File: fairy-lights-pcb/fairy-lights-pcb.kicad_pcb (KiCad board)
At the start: 2 copper layers, 60 x 60 mm, 18 parts, among them J1 Power_Jack, J2 Conn_LED_Strand, J3 Conn_LED_Strand, J4 Conn_LED_Strand, J5 Conn_02x04_Top_Bottom, SW1 SW_PWR, SW2 SW_User, U1 WeMos_D1_mini, U2 TXS0108EPW

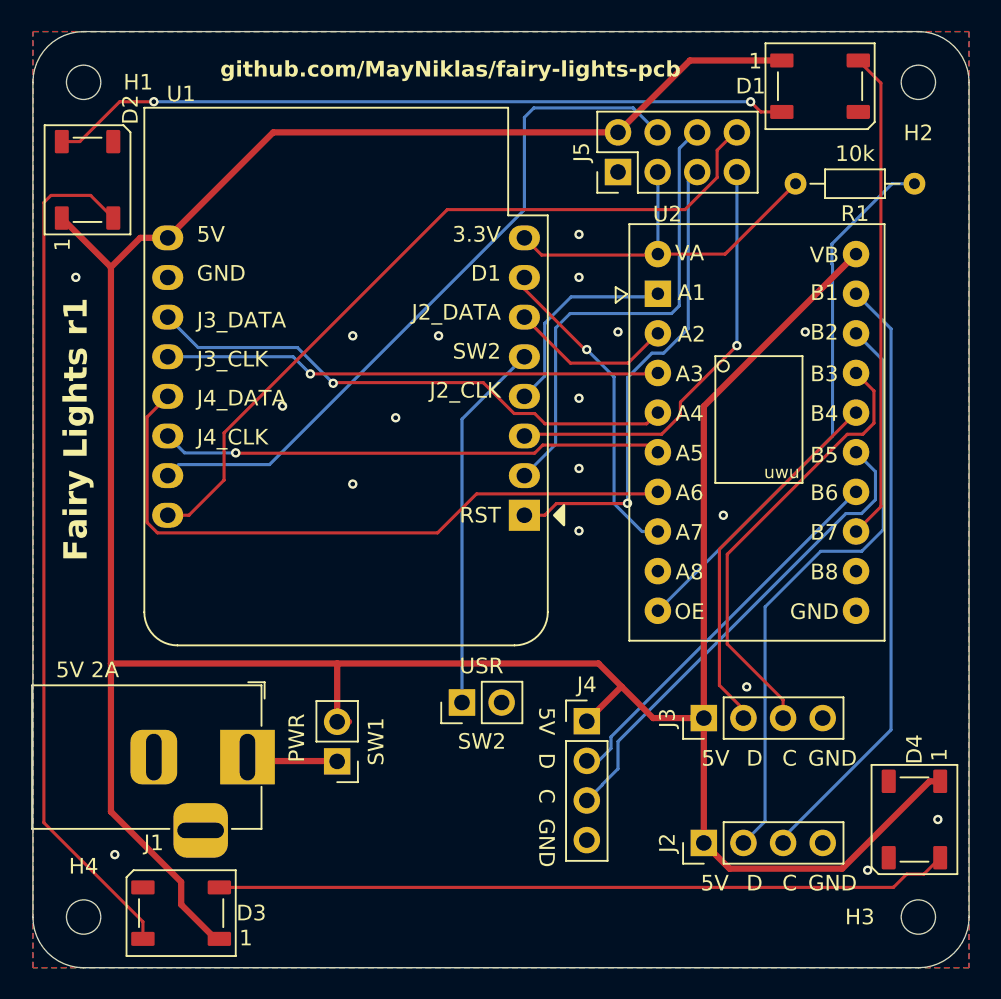
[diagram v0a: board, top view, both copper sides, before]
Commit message: Yeet level shifter; update interfaces
- The level shifter we planned to use seems not to work on a breadboard.
- Driving the LED controllers with 3.3V signals directly instead seems
  to work (although it is out-of-spec or barely at the boundary of what
  is in-spec).
- LED strands are now attached via screw terminals. (Of course, one can
  choose not to populate them and solder wires directly to the pads
  instead.)
- The size of one of the terminals is reduced to three signals, to
  accomodate WS2812 LED strands.
- The thus-free GPIO pin is repurposed to be another switch.
- Changed user switches to tactile vertical push buttons.
- Updated parts list in README.
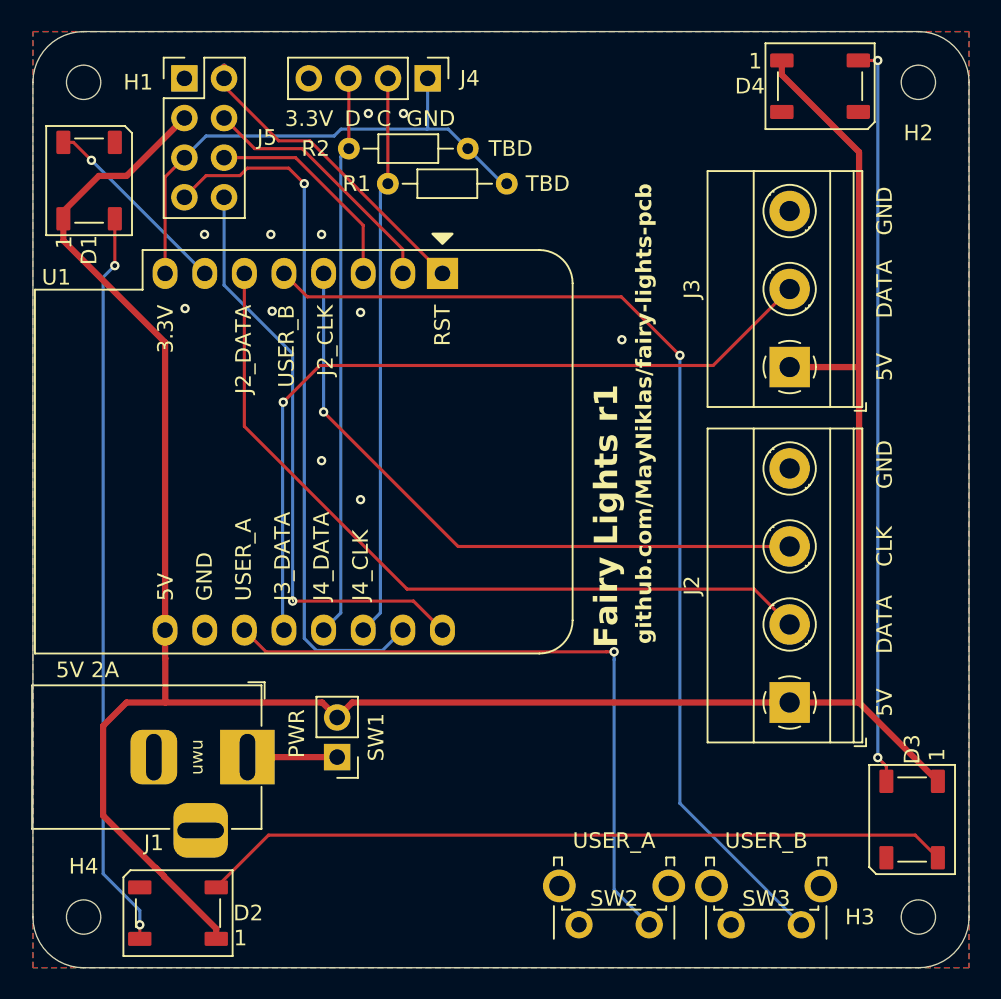
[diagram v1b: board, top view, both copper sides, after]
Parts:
- removed U2: TXS0108EPW, CustomLibrary:Texas_TXS0108E_Level_Shifter_Module
- added R2: TBD, Resistor_THT:R_Axial_DIN0204_L3.6mm_D1.6mm_P7.62mm_Horizontal, F.Cu at (87.9, 67.5)
- added SW3: USER_B, Button_Switch_THT:SW_Tactile_SPST_Angled_PTS645Vx31-2LFS, F.Cu at (109.2, 117.2)
- J2: value Conn_LED_Strand -> Conn_LED_Strand_SPI; footprint Connector_PinHeader_2.54mm:PinHeader_1x04_P2.54mm_Vertical -> TerminalBlock_Phoenix:TerminalBlock_Phoenix_MKDS-1,5-4_1x04_P5.00mm_Horizontal
- J3: value Conn_LED_Strand -> Conn_LED_Strand_WS2812; footprint Connector_PinHeader_2.54mm:PinHeader_1x04_P2.54mm_Vertical -> TerminalBlock_Phoenix:TerminalBlock_Phoenix_MKDS-1,5-3_1x03_P5.00mm_Horizontal
- J4: value Conn_LED_Strand -> Conn_I2C
- R1: value 10k -> TBD
- SW2: value SW_User -> USER_A; footprint Connector_PinHeader_2.54mm:PinHeader_1x02_P2.54mm_Vertical -> Button_Switch_THT:SW_Tactile_SPST_Angled_PTS645Vx31-2LFS
- moved D4 47.4 mm to (110.5, 63.5), turned to 0 degrees
- moved D2 47.4 mm to (69.3, 116.5), turned to 180 degrees
- moved D1 47.2 mm to (63.6, 69.5), turned to 90 degrees
- moved D3 47.2 mm to (116.3, 110.5), turned to -90 degrees
- moved J4 42.4 mm to (85.3, 63.0), turned to -90 degrees
- moved R1 33.8 mm to (82.8, 69.8), turned to 0 degrees
- moved J5 28.4 mm to (69.7, 63.0), turned to 0 degrees
- moved J3 23.2 mm to (108.5, 81.5)
- moved SW2 18.6 mm to (99.5, 117.2), turned to 180 degrees
- moved U1 16.4 mm to (86.2, 75.5), turned to -90 degrees
- moved J2 10.5 mm to (108.5, 103.0)
- moved SW1 0.28 mm to (79.5, 106.5)
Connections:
- J3 pad 3: Net-(J3-CLK) -> GND
- J4 pad 1: +5V -> +3.3V
- J4 pad 2: Net-(J4-DATA) -> Net-(J4-CLK)
- J4 pad 3: Net-(J4-CLK) -> Net-(J4-DATA)
- J5 pad 2: +5V -> UC_RST
- J5 pad 3: +3.3V -> +5V
- J5 pad 4: UC_RX -> UC_A0
- J5 pad 5: UC_RST -> +3.3V
- J5 pad 6: UC_A0 -> UC_D0
- J5 pad 7: UC_D0 -> UC_RX
- R1 pad 1: Net-(U2-OE) -> Net-(J4-CLK)
- SW2 pad 1: Net-(U1-MISO/D6) -> Net-(U1-D4)
- U1 pad 12: Net-(U1-D3) -> Net-(J3-DATA)
- U1 pad 13: Net-(U1-SDA/D2) -> Net-(J4-DATA)
- U1 pad 14: Net-(U1-SCL/D1) -> Net-(J4-CLK)
- U1 pad 4: Net-(U1-SCK/D5) -> Net-(J2-CLK)
- U1 pad 6: Net-(U1-MOSI/D7) -> Net-(J2-DATA)
- U1 pad 7: Net-(U1-CS/D8) -> Net-(D1-DIN)
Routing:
- net Net-(U1-MISO/D6): track 23.8 -> 67.3 mm, vias 0 -> 1
- net Net-(U1-SDA/D2): track 42.7 -> 0.00 mm
- net +5V: track 205.3 -> 165.9 mm
- net Net-(U2-OE): track 35.1 -> 0.00 mm
- net Net-(U1-SCL/D1): track 32.3 -> 0.00 mm, vias 1 -> 0
- net Net-(U1-D3): track 31.9 -> 0.00 mm, vias 1 -> 0
- net Net-(J3-CLK): track 28.6 -> 0.00 mm
- net Net-(J3-DATA): track 23.8 -> 50.1 mm, vias 0 -> 1
- net Net-(U1-CS/D8): track 20.5 -> 0.00 mm, vias 1 -> 0
- net Net-(D1-DIN): track 31.5 -> 12.5 mm, vias 0 -> 1
- net UC_A0: track 30.5 -> 16.5 mm
- net UC_D0: track 27.6 -> 13.8 mm, vias 1 -> 0
- net Net-(U1-SCK/D5): track 13.3 -> 0.00 mm
- net Net-(J2-DATA): track 38.6 -> 50.0 mm
- net UC_TX: track 49.4 -> 38.1 mm, vias 0 -> 1
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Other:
- board text added: "CLK"
- board text added: "DATA"
- board text added: "USER_A"
- board text added: "USER_B"
- board text removed: "D1"
- board text removed: "J3_CLK"
- board text removed: "SW2"
- board text removed: "USR"

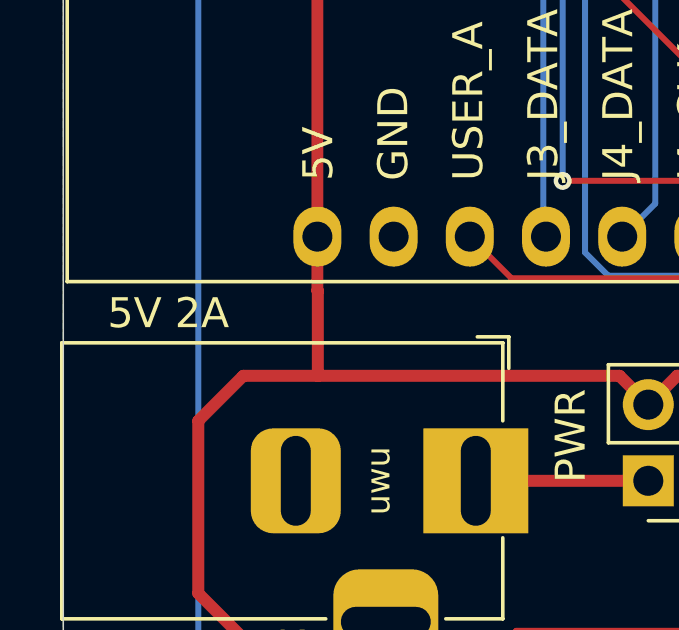
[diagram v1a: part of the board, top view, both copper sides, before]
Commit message: Ground the mounting pins of the buttons
Also tweaks the location of the "5V 2A" label.
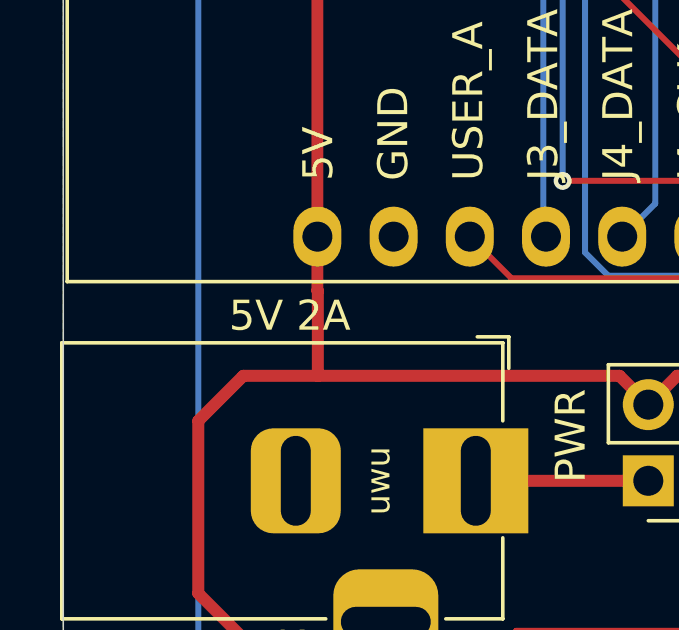
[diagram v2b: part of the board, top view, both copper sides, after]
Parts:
- SW2, SW3: footprint Button_Switch_THT:SW_Tactile_SPST_Angled_PTS645Vx31-2LFS -> CustomLibrary:SW_Tactile_SPST_Angled_PTS645Vx31-2LFS_2MP
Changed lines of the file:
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@@
 		)
 	)
-	(footprint "Button_Switch_THT:SW_Tactile_SPST_Angled_PTS645Vx31-2LFS"
+	(footprint "CustomLibrary:SW_Tactile_SPST_Angled_PTS645Vx31-2LFS_2MP"
 		(layer "F.Cu")
 		(at 99.5 117.2441 180)
@@
 		(tags "tactile switch SPST angled PTS645VL31-2 LFS C&K Button")
 		(property "Reference" "SW2"
-			(at 2.25 1.68 0)
+			(at 2.25 1.68 180)
 			(layer "F.SilkS")
 			(effects
@@
 		)
 		(property "Value" "USER_A"
-			(at 2.25 5.38988 0)
+			(at 2.25 5.38988 180)
 			(layer "F.SilkS")
 			(effects
@@
 			)
 		)
-		(property "Footprint" "Button_Switch_THT:SW_Tactile_SPST_Angled_PTS645Vx31-2LFS"
+		(property "Footprint" "CustomLibrary:SW_Tactile_SPST_Angled_PTS645Vx31-2LFS_2MP"
 			(at 0 0 180)
 			(unlocked yes)
@@
 			)
 		)
-		(property "Description" "Push button switch, generic, two pins"
+		(property "Description" "Generic push-button switch, two contact pins and shield pin(s)"
 			(at 0 0 180)
 			(unlocked yes)
@@
 		)
 		(fp_text user "${REFERENCE}"
-			(at 2.25 1.68 0)
+			(at 2.25 1.68 180)
 			(layer "F.Fab")
 			(effects
@@
 			)
 		)
-		(pad "" thru_hole circle
-			(at -1.25 2.49 180)
-			(size 2.1 2.1)
-			(drill 1.3)
-			(layers "*.Cu" "*.Mask")
-			(remove_unused_layers no)
-		)
-		(pad "" thru_hole circle
-			(at 5.76 2.49 180)
-			(size 2.1 2.1)
-			(drill 1.3)
-			(layers "*.Cu" "*.Mask")
-			(remove_unused_layers no)
-		)
 		(pad "1" thru_hole circle
 			(at 0 0 180)
@@
 			(pintype "passive")
 		)
+		(pad "3" thru_hole circle
+			(at -1.25 2.49 180)
+			(size 2.1 2.1)
+			(drill 1.3)
+			(layers "*.Cu" "*.Mask")
+			(remove_unused_layers no)
+			(net 2 "GND")
+			(pinfunction "SH1")
+			(pintype "passive")
+		)
+		(pad "4" thru_hole circle
+			(at 5.76 2.49 180)
+			(size 2.1 2.1)
+			(drill 1.3)
+			(layers "*.Cu" "*.Mask")
+			(remove_unused_layers no)
+			(net 2 "GND")
+			(pinfunction "SH2")
+			(pintype "passive")
+		)
 		(model "${KICAD8_3DMODEL_DIR}/Button_Switch_THT.3dshapes/SW_Tactile_SPST_Angled_PTS645Vx31-2LFS.wrl"
 			(offset
@@
 		)
 	)
-	(footprint "Button_Switch_THT:SW_Tactile_SPST_Angled_PTS645Vx31-2LFS"
+	(footprint "CustomLibrary:SW_Tactile_SPST_Angled_PTS645Vx31-2LFS_2MP"
 		(layer "F.Cu")
 		(at 109.25 117.25 180)
@@
 		(tags "tactile switch SPST angled PTS645VL31-2 LFS C&K Button")
 		(property "Reference" "SW3"
-			(at 2.25 1.68 0)
+			(at 2.25 1.68 180)
 			(layer "F.SilkS")
 			(effects
@@
 		)
 		(property "Value" "USER_B"
-			(at 2.25 5.38988 0)
+			(at 2.25 5.38988 180)
 			(layer "F.SilkS")
 			(effects
@@
 			)
 		)
-		(property "Footprint" "Button_Switch_THT:SW_Tactile_SPST_Angled_PTS645Vx31-2LFS"
+		(property "Footprint" "CustomLibrary:SW_Tactile_SPST_Angled_PTS645Vx31-2LFS_2MP"
 			(at 0 0 180)
 			(unlocked yes)
@@
 			)
 		)
-		(property "Description" "Push button switch, generic, two pins"
+		(property "Description" "Generic push-button switch, two contact pins and shield pin(s)"
 			(at 0 0 180)
 			(unlocked yes)
@@
 		)
 		(fp_text user "${REFERENCE}"
-			(at 2.25 1.68 0)
+			(at 2.25 1.68 180)
 			(layer "F.Fab")
 			(effects
@@
 			)
 		)
-		(pad "" thru_hole circle
-			(at -1.25 2.49 180)
-			(size 2.1 2.1)
-			(drill 1.3)
-			(layers "*.Cu" "*.Mask")
-			(remove_unused_layers no)
-		)
-		(pad "" thru_hole circle
-			(at 5.76 2.49 180)
-			(size 2.1 2.1)
-			(drill 1.3)
-			(layers "*.Cu" "*.Mask")
-			(remove_unused_layers no)
-		)
 		(pad "1" thru_hole circle
 			(at 0 0 180)
@@
 			(pintype "passive")
 		)
+		(pad "3" thru_hole circle
+			(at -1.25 2.49 180)
+			(size 2.1 2.1)
+			(drill 1.3)
+			(layers "*.Cu" "*.Mask")
+			(remove_unused_layers no)
+			(net 2 "GND")
+			(pinfunction "SH1")
+			(pintype "passive")
+		)
+		(pad "4" thru_hole circle
+			(at 5.76 2.49 180)
+			(size 2.1 2.1)
+			(drill 1.3)
+			(layers "*.Cu" "*.Mask")
+			(remove_unused_layers no)
+			(net 2 "GND")
+			(pinfunction "SH2")
+			(pintype "passive")
+		)
 		(model "${KICAD8_3DMODEL_DIR}/Button_Switch_THT.3dshapes/SW_Tactile_SPST_Angled_PTS645Vx31-2LFS.wrl"
 			(offset
@@
 	)
 	(gr_text "5V 2A"
-		(at 63.5 101.5 0)
+		(at 67.55 101 0)
 		(layer "F.SilkS")
 		(effects
@@
 				(thickness 0.1)
 			)
-			(justify bottom)
 		)
 	)

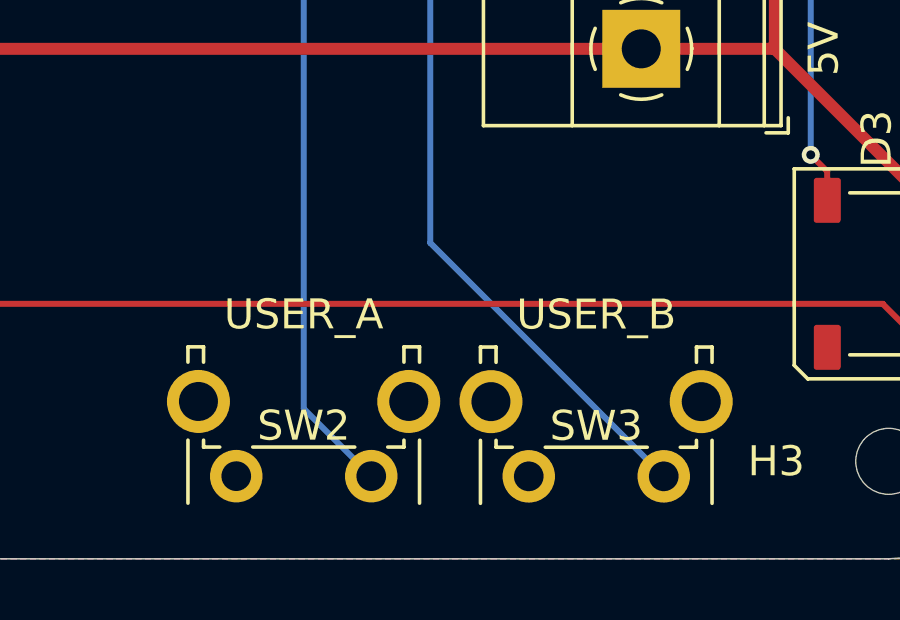
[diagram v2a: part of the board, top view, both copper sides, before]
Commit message: Tweak push button footprint
Oh, hey, one can assign multiple footprint pads to the same schematic
pin!
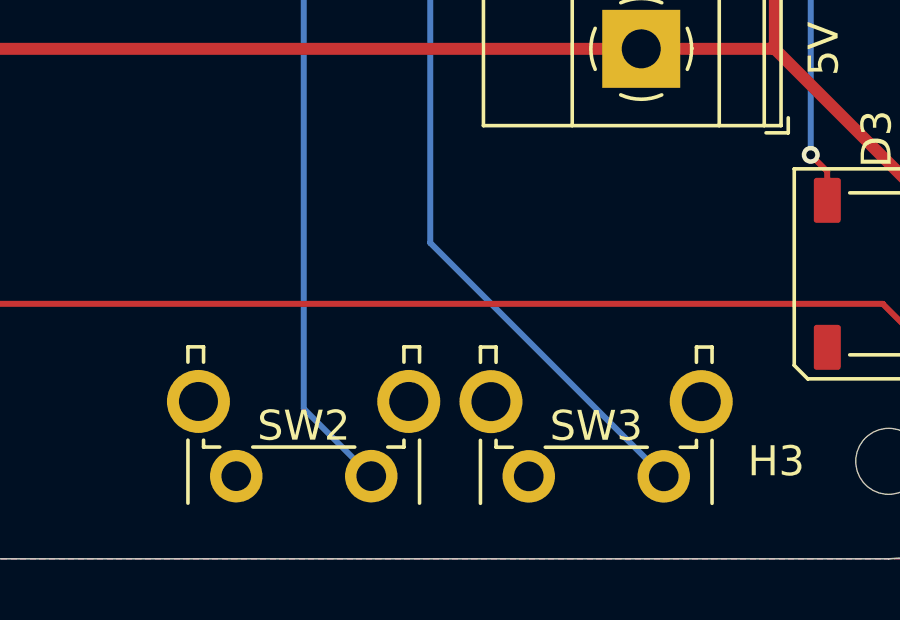
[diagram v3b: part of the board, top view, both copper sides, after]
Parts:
- SW2, SW3: footprint CustomLibrary:SW_Tactile_SPST_Angled_PTS645Vx31-2LFS_2MP -> CustomLibrary:SW_Tactile_SPST_Angled_PTS645Vx31-2LFS_SH
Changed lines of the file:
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@@
 		)
 	)
-	(footprint "CustomLibrary:SW_Tactile_SPST_Angled_PTS645Vx31-2LFS_2MP"
+	(footprint "CustomLibrary:SW_Tactile_SPST_Angled_PTS645Vx31-2LFS_SH"
 		(layer "F.Cu")
 		(at 99.5 117.2441 180)
-		(descr "tactile switch SPST right angle, PTS645VL31-2 LFS")
+		(descr "tactile switch SPST right angle, PTS645VL31-2 LFS, with shield pads")
 		(tags "tactile switch SPST angled PTS645VL31-2 LFS C&K Button")
 		(property "Reference" "SW2"
@@
 		(property "Value" "USER_A"
 			(at 2.25 5.38988 180)
-			(layer "F.SilkS")
+			(layer "F.Fab")
 			(effects
 				(font
@@
 			)
 		)
-		(property "Footprint" "CustomLibrary:SW_Tactile_SPST_Angled_PTS645Vx31-2LFS_2MP"
+		(property "Footprint" "CustomLibrary:SW_Tactile_SPST_Angled_PTS645Vx31-2LFS_SH"
 			(at 0 0 180)
 			(unlocked yes)
@@
 			(pintype "passive")
 		)
-		(pad "3" thru_hole circle
+		(pad "SH" thru_hole circle
 			(at -1.25 2.49 180)
 			(size 2.1 2.1)
@@
 			(remove_unused_layers no)
 			(net 2 "GND")
-			(pinfunction "SH1")
+			(pinfunction "B")
 			(pintype "passive")
 		)
-		(pad "4" thru_hole circle
+		(pad "SH" thru_hole circle
 			(at 5.76 2.49 180)
 			(size 2.1 2.1)
@@
 			(remove_unused_layers no)
 			(net 2 "GND")
-			(pinfunction "SH2")
+			(pinfunction "B")
 			(pintype "passive")
 		)
@@
 		)
 	)
-	(footprint "CustomLibrary:SW_Tactile_SPST_Angled_PTS645Vx31-2LFS_2MP"
+	(footprint "CustomLibrary:SW_Tactile_SPST_Angled_PTS645Vx31-2LFS_SH"
 		(layer "F.Cu")
 		(at 109.25 117.25 180)
-		(descr "tactile switch SPST right angle, PTS645VL31-2 LFS")
+		(descr "tactile switch SPST right angle, PTS645VL31-2 LFS, with shield pads")
 		(tags "tactile switch SPST angled PTS645VL31-2 LFS C&K Button")
 		(property "Reference" "SW3"
@@
 		(property "Value" "USER_B"
 			(at 2.25 5.38988 180)
-			(layer "F.SilkS")
+			(layer "F.Fab")
 			(effects
 				(font
@@
 			)
 		)
-		(property "Footprint" "CustomLibrary:SW_Tactile_SPST_Angled_PTS645Vx31-2LFS_2MP"
+		(property "Footprint" "CustomLibrary:SW_Tactile_SPST_Angled_PTS645Vx31-2LFS_SH"
 			(at 0 0 180)
 			(unlocked yes)
@@
 			(pintype "passive")
 		)
-		(pad "3" thru_hole circle
+		(pad "SH" thru_hole circle
 			(at -1.25 2.49 180)
 			(size 2.1 2.1)
@@
 			(remove_unused_layers no)
 			(net 2 "GND")
-			(pinfunction "SH1")
+			(pinfunction "B")
 			(pintype "passive")
 		)
-		(pad "4" thru_hole circle
+		(pad "SH" thru_hole circle
 			(at 5.76 2.49 180)
 			(size 2.1 2.1)
@@
 			(remove_unused_layers no)
 			(net 2 "GND")
-			(pinfunction "SH2")
+			(pinfunction "B")
 			(pintype "passive")
 		)
